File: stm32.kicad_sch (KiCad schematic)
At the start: 0 parts

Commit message: Ajout des deux moteurs
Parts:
- added C19, C22: 100nF, Capacitor_SMD:C_0805_2012Metric, symbol local:C_0402
- added C21: 1µF, Capacitor_SMD:C_0805_2012Metric, symbol local:C_0402
- added C23: 4.7µF, Capacitor_SMD:C_0805_2012Metric, symbol local:C_0402
- added S1: Push_button, local:Push_button, symbol local:Push_button
- added U4: STM32G431KBT6, local:QFP80P900X900X160-32N, symbol local:STM32G431KBT6
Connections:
- new net GND: C19.1, C21.1, C22.1, C23.1, U4.14 (VSSA), U4.16 (VSS), U4.32 (VSS)
- new net VDD: C19.2, C21.2, C22.2, C23.2, U4.1 (VDD), U4.15 (VDDA/VREF+), U4.17 (VDD)

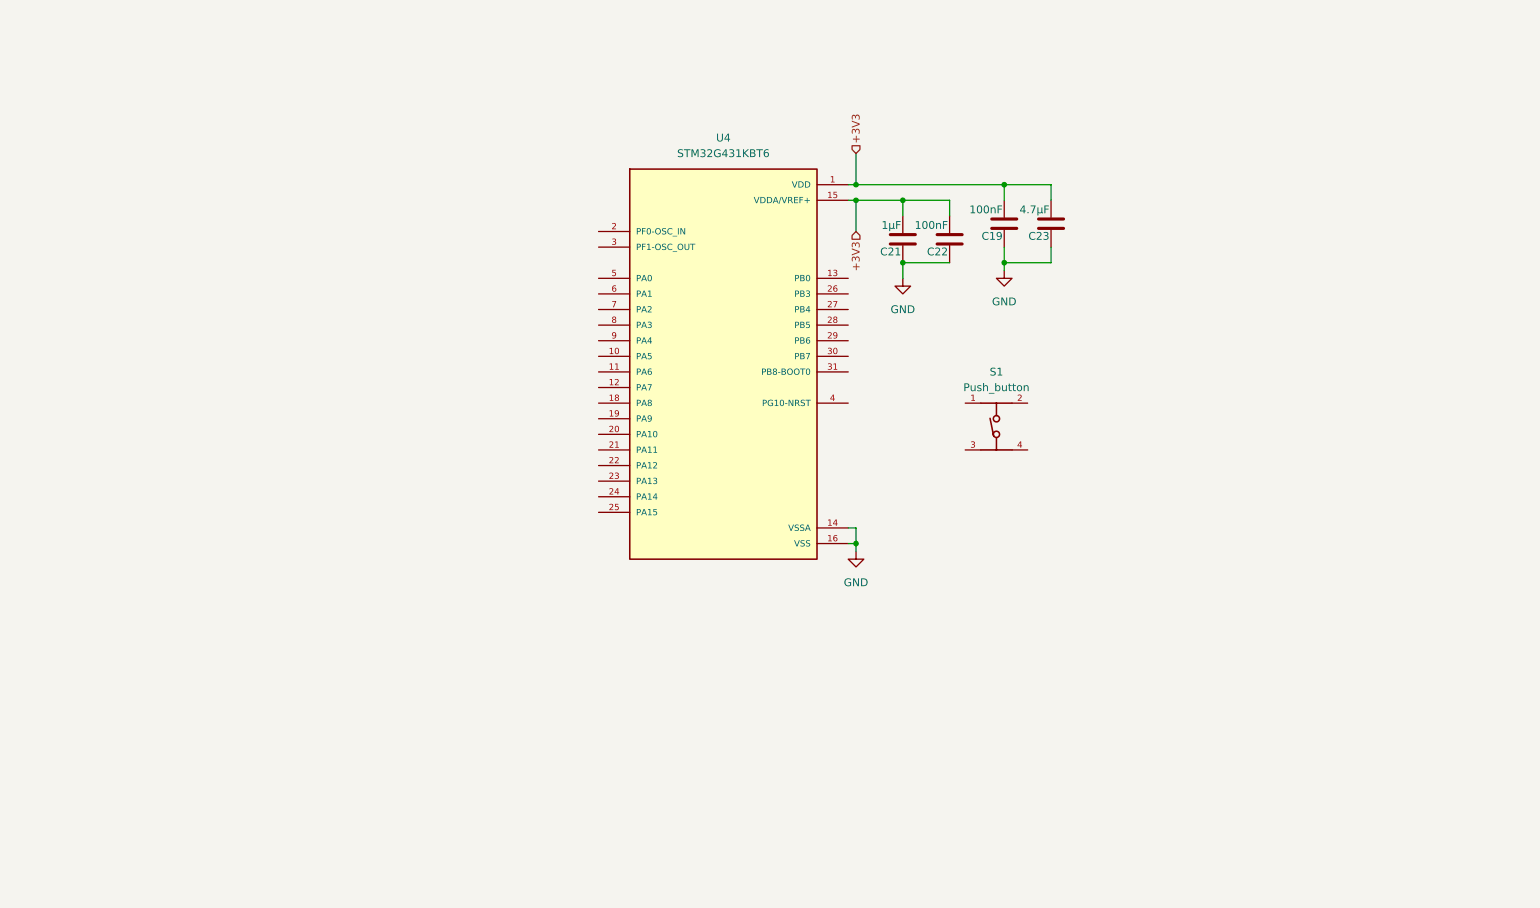
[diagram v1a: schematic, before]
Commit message: Version 0. Schémas finalisés. Mise à jour des résistances en série E12. Réduction de la BOM.
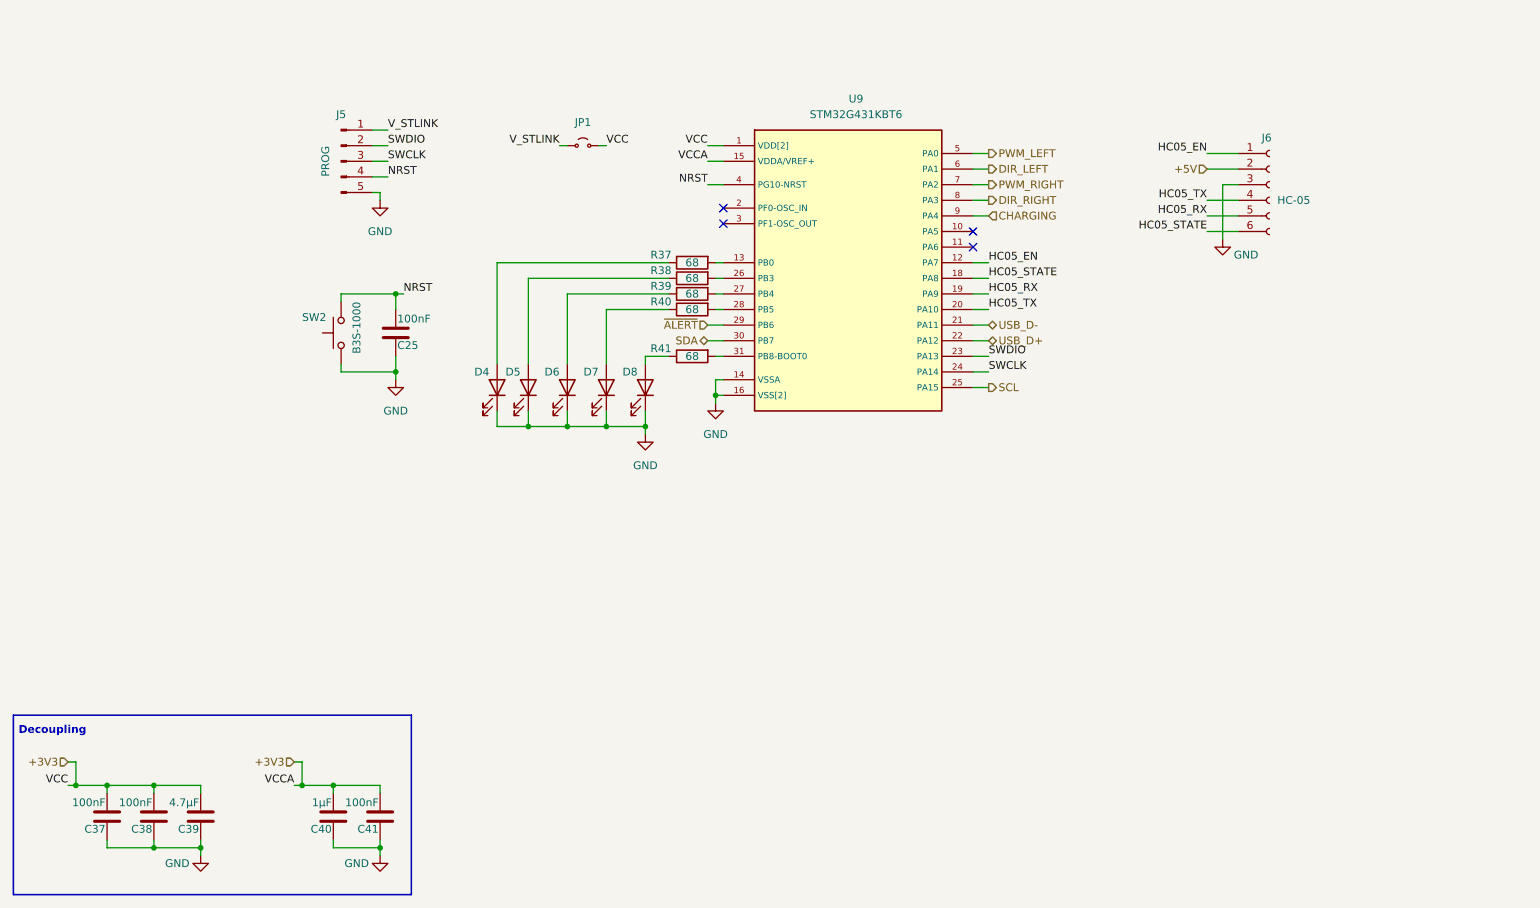
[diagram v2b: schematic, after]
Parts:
- removed C19, C22: 100nF, Capacitor_SMD:C_0805_2012Metric, symbol local:C_0402
- removed C21: 1µF, Capacitor_SMD:C_0805_2012Metric, symbol local:C_0402
- removed C23: 4.7µF, Capacitor_SMD:C_0805_2012Metric, symbol local:C_0402
- removed S1: Push_button, local:Push_button, symbol local:Push_button
- added C25, C37, C38, C41: 100nF, Capacitor_SMD:C_0805_2012Metric, symbol local:C_0402
- added C39: 4.7µF, Capacitor_SMD:C_0805_2012Metric, symbol local:C_0402
- added C40: 1µF, Capacitor_SMD:C_0805_2012Metric, symbol local:C_0402
- added D4, D5, D6, D7, D8: LED, symbol Device:LED
- added J5: PROG, symbol Connector:Conn_01x05_Pin
- added J6: HC-05, symbol Connector:Conn_01x06_Socket
- added JP1: Jumper_2_Small_Open, symbol Jumper:Jumper_2_Small_Open
- added R37, R38, R39, R40, R41: 68, Resistor_SMD:R_0805_2012Metric, symbol local:R
- added SW2: B3S-1000, local:SW_SPST_B3S-1000, symbol Switch:SW_Push
- renumbered U4 to U9
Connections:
- net GND: now also C25.1, C37.1, C38.1, C39.1, C40.1, C41.1, D4.1 (K), D5.1 (K), D6.1 (K), D7.1 (K), D8.1 (K), J5.5 (Pin_5), J6.3 (Pin_3), SW2.1
- net VDD: now also C37.2, C38.2, C39.2, C40.2, C41.2, JP1.2 (B)
- net HC05_EN: now reaches U9.12 (PA7)
- net HC05_EN: now also J6.1 (Pin_1)
- net at U9.13 (PB0): now also R37.2
- net HC05_STATE: now reaches U9.18 (PA8)
- net HC05_STATE: now also J6.6 (Pin_6)
- net HC05_RX: now reaches U9.19 (PA9)
- net HC05_RX: now also J6.5 (Pin_5)
- net HC05_TX: now reaches U9.20 (PA10)
- net HC05_TX: now also J6.4 (Pin_4)
- net USB_D-: now reaches U9.21 (PA11)
- net USB_D+: now reaches U9.22 (PA12)
- net SWDIO: now reaches U9.23 (PA13)
- net SWDIO: now also J5.2 (Pin_2)
- net SWCLK: now reaches U9.24 (PA14)
- net SWCLK: now also J5.3 (Pin_3)
- net SCL: now reaches U9.25 (PA15)
- net at U9.26 (PB3): now also R38.2
- net at U9.27 (PB4): now also R39.2
- net at U9.28 (PB5): now also R40.2
- net ~{ALERT}: now reaches U9.29 (PB6)
- net SDA: now reaches U9.30 (PB7)
- net at U9.31 (PB8-BOOT0): now also R41.2
- net NRST: now reaches U9.4 (PG10-NRST)
- net NRST: now also C25.2, J5.4 (Pin_4), SW2.2
- net PWM_LEFT: now reaches U9.5 (PA0)
- net DIR_LEFT: now reaches U9.6 (PA1)
- net PWM_RIGHT: now reaches U9.7 (PA2)
- net DIR_RIGHT: now reaches U9.8 (PA3)
- net CHARGING: now reaches U9.9 (PA4)
- new net: D6.2 (A), R39.1
- new net: D5.2 (A), R38.1
- new net: D4.2 (A), R37.1
- new net: D8.2 (A), R41.1
- new net: D7.2 (A), R40.1
- new net +5V: J6.2 (Pin_2)
- new net V_STLINK: J5.1 (Pin_1), JP1.1 (A)
- no-connect marks 0 -> 4
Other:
- note added: "Decoupling"
- moved on the sheet: U9

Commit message: Minor Schematics update
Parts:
- removed D4, D5: LED, symbol Device:LED
- removed R37, R38: 68, Resistor_SMD:R_0805_2012Metric, symbol local:R
- added C42, C48: 100nF, Capacitor_SMD:C_0603_1608Metric, symbol local:C
- added J10: Conn_DET_RIGHT, Connector_PinHeader_2.54mm:PinHeader_1x02_P2.54mm_Vertical, symbol Connector:Conn_01x02_Pin
- added J9: Conn_DET_LEFT, Connector_PinHeader_2.54mm:PinHeader_1x02_P2.54mm_Vertical, symbol Connector:Conn_01x02_Pin
- added R48, R50: 47k, Resistor_SMD:R_0603_1608Metric, symbol local:R
- added R51, R52, R53: 4.7k, Resistor_SMD:R_0603_1608Metric, symbol local:R
- added SW3, SW4: B3S-1000, local:SW_SPST_B3S-1000, symbol Switch:SW_Push
- C41: renamed from C25; footprint Capacitor_SMD:C_0805_2012Metric -> Capacitor_SMD:C_0603_1608Metric; symbol local:C_0402 -> local:C
- C43: renamed from C37; footprint Capacitor_SMD:C_0805_2012Metric -> Capacitor_SMD:C_0603_1608Metric; symbol local:C_0402 -> local:C
- C44: renamed from C38; footprint Capacitor_SMD:C_0805_2012Metric -> Capacitor_SMD:C_0603_1608Metric; symbol local:C_0402 -> local:C
- C45: renamed from C39; symbol local:C_0402 -> local:C
- C46: renamed from C40; footprint Capacitor_SMD:C_0805_2012Metric -> Capacitor_SMD:C_0603_1608Metric; symbol local:C_0402 -> local:C
- C47: renamed from C41; footprint Capacitor_SMD:C_0805_2012Metric -> Capacitor_SMD:C_0603_1608Metric; symbol local:C_0402 -> local:C
- D5: renamed from D6; footprint (none) -> LED_SMD:LED_0603_1608Metric
- D6: renamed from D7; footprint (none) -> LED_SMD:LED_0603_1608Metric
- D7: renamed from D8; footprint (none) -> LED_SMD:LED_0603_1608Metric
- J7: renamed from J6; footprint (none) -> Connector_PinSocket_2.54mm:PinSocket_1x06_P2.54mm_Vertical
- J8: renamed from J5; footprint (none) -> Connector_PinHeader_2.54mm:PinHeader_1x05_P2.54mm_Vertical
- JP1: footprint (none) -> Connector_PinHeader_2.54mm:PinHeader_1x02_P2.54mm_Vertical
- R46: renamed from R39; footprint Resistor_SMD:R_0805_2012Metric -> Resistor_SMD:R_0603_1608Metric
- R47: renamed from R40; footprint Resistor_SMD:R_0805_2012Metric -> Resistor_SMD:R_0603_1608Metric
- R49: renamed from R41; footprint Resistor_SMD:R_0805_2012Metric -> Resistor_SMD:R_0603_1608Metric
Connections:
- net CHARGING: now also U9.10 (PA5); no longer U9.9 (PA4)
- net DIR_LEFT: now also U9.3 (PF1-OSC_OUT); no longer U9.6 (PA1)
- net GND: now also C42.1, C48.1, J10.2 (Pin_2), J9.2 (Pin_2), SW3.1, SW4.1
- net PWM_LEFT: now also U9.2 (PF0-OSC_IN); no longer U9.5 (PA0)
- net SCL: now also R53.1
- net SDA: now also R52.1
- net VDD: now also R48.1, R50.1, R51.2, R52.2, R53.2
- net ~{ALERT}: now also R51.1
- net DETECT_RIGHT: now reaches U9.26 (PB3)
- net DETECT_RIGHT: now also C48.2, J10.1 (Pin_1), R50.2, SW4.2
- net DETECT_LEFT: now reaches U9.13 (PB0)
- net DETECT_LEFT: now also C42.2, J9.1 (Pin_1), R48.2, SW3.2
- net ENC_B_RIGHT: now reaches U9.11 (PA6)
- new net ENC_A_LEFT: U9.5 (PA0)
- new net ENC_A_RIGHT: U9.9 (PA4)
- new net ENC_B_LEFT: U9.6 (PA1)
- no-connect marks 4 -> 0
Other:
- note added: "Bluetooth"
- note added: "DNP"
- note added: "Détection d'un contact"
- note added: "Prog & RESET"
- note added: "STM32"
- note added: "VDD"
- note added: "VDDA"
- moved on the sheet: C41, C43, C44, C45, C46, C47, D5, D6, D7, J7, J8, JP1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

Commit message: Modification mineur du schéma, ajout du PCB V1
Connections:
- net DETECT_LEFT: now also J9.2 (Pin_2); no longer J9.1 (Pin_1)
- net DETECT_RIGHT: now also J10.2 (Pin_2); no longer J10.1 (Pin_1)
- net DIR_LEFT: now also U9.8 (PA3); no longer U9.3 (PF1-OSC_OUT)
- net DIR_RIGHT: now also U9.3 (PF1-OSC_OUT); no longer U9.8 (PA3)
- net GND: now also J10.1 (Pin_1), J8.1 (Pin_1), J9.1 (Pin_1); no longer J10.2 (Pin_2), J8.5 (Pin_5), J9.2 (Pin_2)
- net NRST: now also J8.2 (Pin_2); no longer J8.4 (Pin_4)
- net PWM_LEFT: now also U9.7 (PA2); no longer U9.2 (PF0-OSC_IN)
- net PWM_RIGHT: now also U9.2 (PF0-OSC_IN); no longer U9.7 (PA2)
- net SWDIO: now also J8.4 (Pin_4); no longer J8.2 (Pin_2)
- net V_STLINK: now also J8.5 (Pin_5); no longer J8.1 (Pin_1)

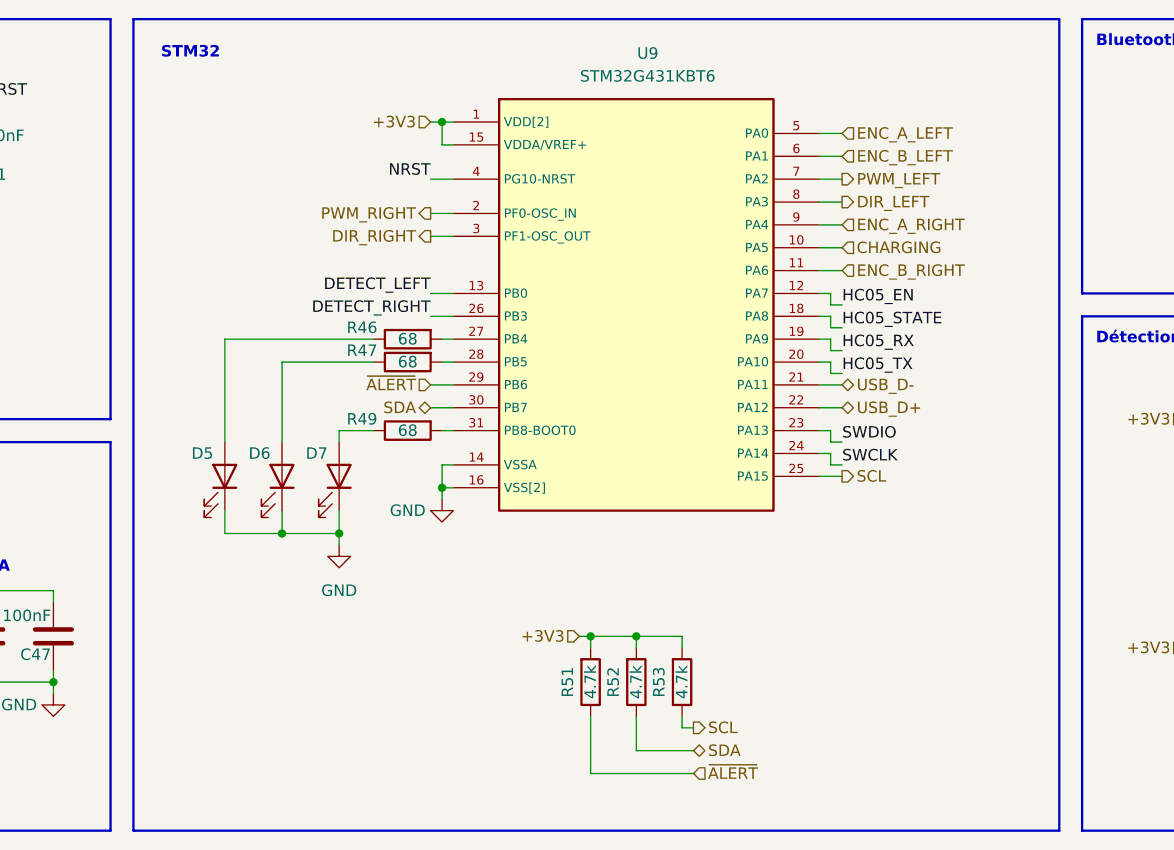
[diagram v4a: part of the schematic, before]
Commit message: Léger remapping du stm32.
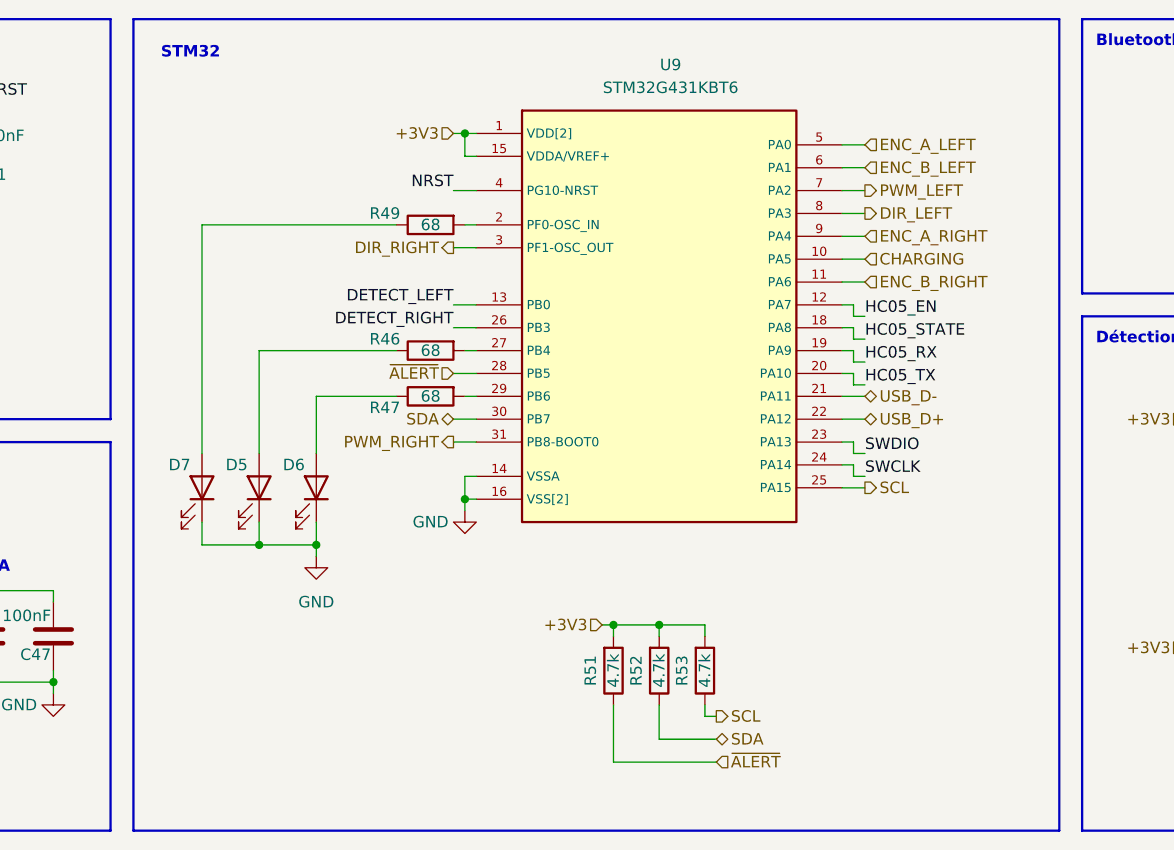
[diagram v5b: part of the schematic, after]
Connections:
- net PWM_RIGHT: now also U9.31 (PB8-BOOT0); no longer U9.2 (PF0-OSC_IN)
- net ~{ALERT}: now also U9.28 (PB5); no longer U9.29 (PB6)
- net at R47.2: now also U9.29 (PB6); no longer U9.28 (PB5)
- net at R49.2: now also U9.2 (PF0-OSC_IN); no longer U9.31 (PB8-BOOT0)
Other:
- moved on the sheet: D5, D6, R46, R47, R51, R52, R53, U9
